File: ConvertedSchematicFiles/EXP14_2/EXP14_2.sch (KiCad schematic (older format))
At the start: 11 parts

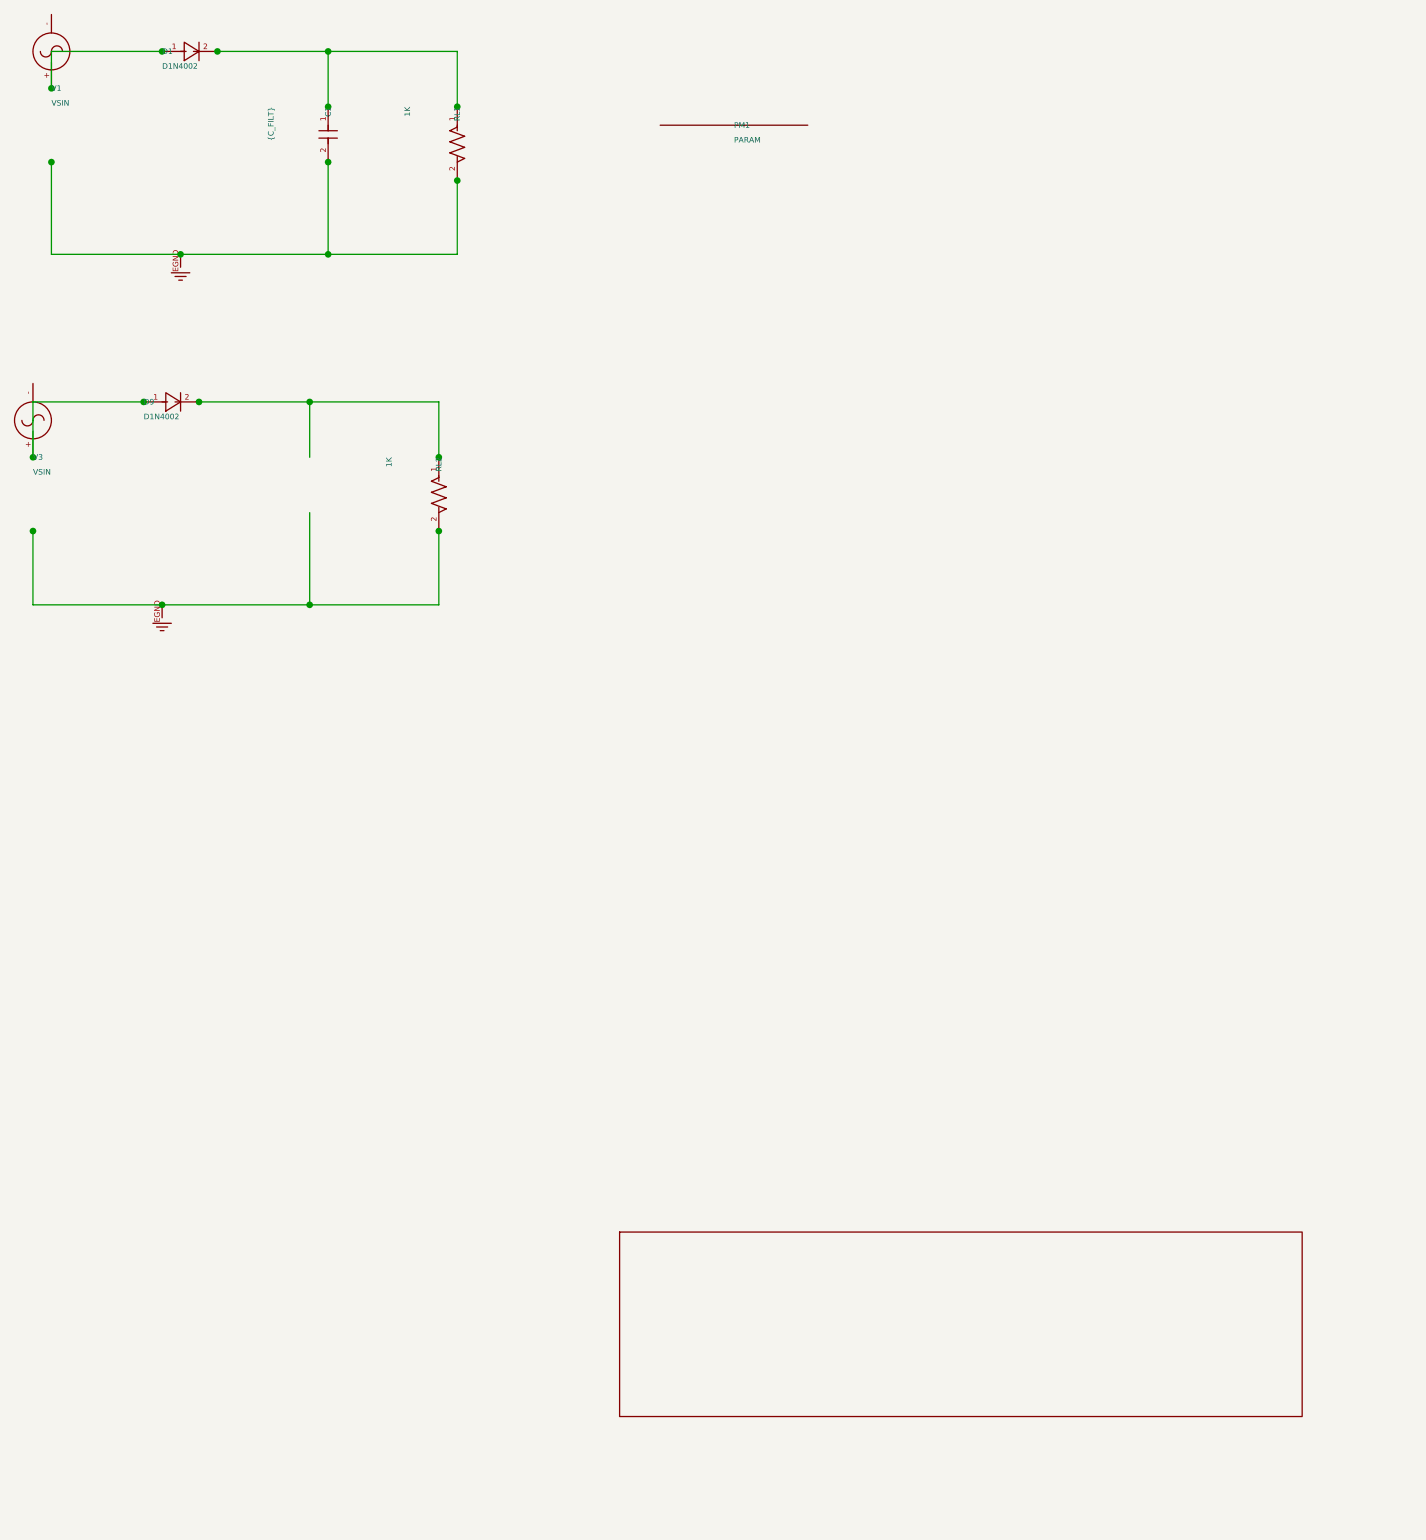
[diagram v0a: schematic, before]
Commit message: Excluded some components. These no longer appear after conversion. When calling shell commands, filenames are in "quotes"
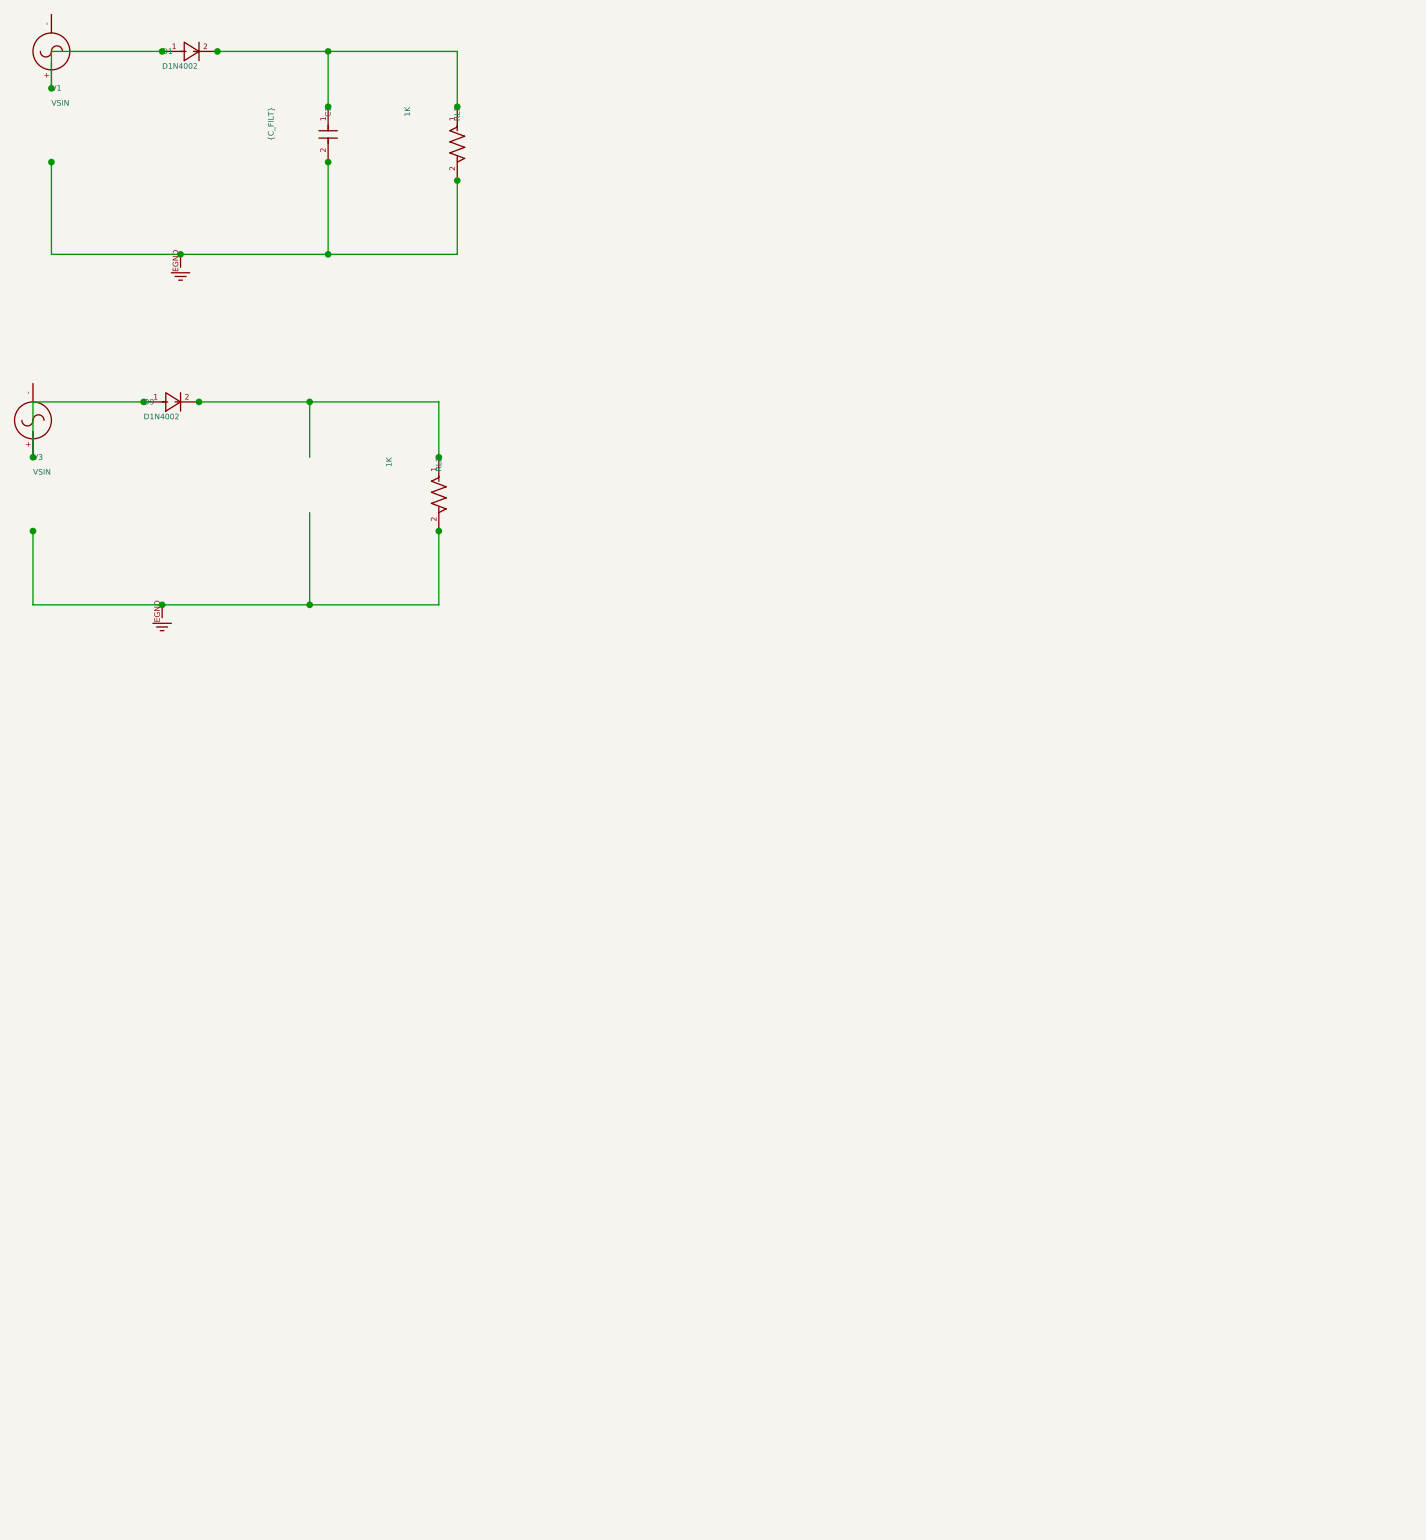
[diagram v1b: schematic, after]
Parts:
- removed PM1: PARAM, symbol PARAM_PSPICE
- removed titleblk: titleblk, symbol TITLEBLK_PSPICE
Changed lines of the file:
@@
-	1    0    0    1
-$EndComp
-$Comp
-L PARAM_PSPICE PM1
-U 1 1 29641421
-P 8800 1400
-F 0 "PM1" H 8800 1400 30  0000 L CNN
-F 1 "PARAM" H 8800 1480 30  0000 L CNN
-	1    8800 1400
-	1    0    0    1
-$EndComp
-$Comp
-L TITLEBLK_PSPICE titleblk
-U 1 1 45202362
-P 11880 8400
-F 0 "titleblk" H 23760 16800 30  0001 L CNN
-F 1 "titleblk" H 23760 16880 30  0001 L CNN
-	1    11880 8400
 	1    0    0    1
 $EndComp

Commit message: Ports issue fixed. Now annotation for ports is #PWR? function added "itos"
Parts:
- removed EGND (x2): EGND, symbol EGND_PSPICE
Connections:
- net labels added: EGND
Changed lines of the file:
@@
 $EndDescr
 $Comp
-L EGND_PSPICE EGND
+L EGND_PSPICE #PWR1
 U 1 1 14289383
 P 5800 2100
-F 0 "EGND" H 11600 4200 30  0001 L CNN
+F 0 "#PWR1" H 11600 4200 30  0001 L CNN
 F 1 "EGND" H 11600 4280 30  0001 L CNN
 	1    5800 2100
@@
 $EndComp
 $Comp
-L EGND_PSPICE EGND
+L EGND_PSPICE #PWR2
 U 1 1 46930886
 P 5700 4000
-F 0 "EGND" H 11400 8000 30  0001 L CNN
+F 0 "#PWR2" H 11400 8000 30  0001 L CNN
 F 1 "EGND" H 11400 8080 30  0001 L CNN
 	1    5700 4000

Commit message: Added LICENSE.txt
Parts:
- V1, V3: value VSIN -> SINE
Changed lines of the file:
@@
 $EndDescr
 $Comp
-L EGND_PSPICE #PWR1
+L GND #PWR1
 U 1 1 14289383
 P 5800 2100
@@
 $EndComp
 $Comp
-L EGND_PSPICE #PWR2
+L GND #PWR2
 U 1 1 46930886
 P 5700 4000
@@
 P 5000 3200
 F 0 "V3" H 5000 3200 30  0000 L CNN
-F 1 "VSIN" H 5000 3280 30  0000 L CNN
+F 1 "SINE" H 5000 3280 30  0000 L CNN
 	1    5000 3200
 	1    0    0    1
@@
 P 5100 1200
 F 0 "V1" H 5100 1200 30  0000 L CNN
-F 1 "VSIN" H 5100 1280 30  0000 L CNN
+F 1 "SINE" H 5100 1280 30  0000 L CNN
 	1    5100 1200
 	1    0    0    1

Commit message: Orientation fix. Library components are now inverted, with +ve y axis going up. In Schematic files, +ve y axis is downwards. This is how the KiCad libraries are. As a result of the above fixed, the converted GND is now oriented correctly.
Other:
- moved on the sheet: V1, V3
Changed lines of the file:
@@
 F 1 "EGND" H 11600 4280 30  0001 L CNN
 	1    5800 2100
-	1    0    0    1
+	1    0    0    -1
 $EndComp
 $Comp
@@
 F 1 "EGND" H 11400 8080 30  0001 L CNN
 	1    5700 4000
-	1    0    0    1
+	1    0    0    -1
 $EndComp
 $Comp
@@
 F 1 "{C_FILT}" H 6600 1610 30  0000 L CNN
 	1    6600 1300
-	0    -1    1    0
+	0    1    1    0
 $EndComp
 $Comp
@@
 F 1 "1K" H 7300 1570 30  0000 L CNN
 	1    7300 1300
-	0    -1    1    0
+	0    1    1    0
 $EndComp
 $Comp
@@
 F 1 "D1N4002" H 5600 2980 30  0000 L CNN
 	1    5600 2900
-	1    0    0    1
+	1    0    0    -1
 $EndComp
 $Comp
@@
 F 1 "SINE" H 5000 3280 30  0000 L CNN
 	1    5000 3200
-	1    0    0    1
+	1    0    0    -1
 $EndComp
 $Comp
@@
 F 1 "1K" H 7200 3470 30  0000 L CNN
 	1    7200 3200
-	0    -1    1    0
+	0    1    1    0
 $EndComp
 $Comp
@@
 F 1 "D1N4002" H 5700 1080 30  0000 L CNN
 	1    5700 1000
-	1    0    0    1
+	1    0    0    -1
 $EndComp
 $Comp
@@
 F 1 "SINE" H 5100 1280 30  0000 L CNN
 	1    5100 1200
-	1    0    0    1
+	1    0    0    -1
 $EndComp
 Wire Wire Line

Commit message: Removed the use of exec, wrote basename function, made integration with eSim easier.
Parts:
- added PM1: PARAM, symbol PARAM_PSPICE
- added titleblk: titleblk, symbol titleblk_PSPICE
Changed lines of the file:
@@
-EESchema Schematic File Version 2  date Saturday 26 June 1999 08:39:42 AM IST
+EESchema Schematic File Version 2  date
 LIBS:power
 LIBS:device
@@
 LIBS:contrib
 LIBS:valves
-LIBS:ConvertedSchematicFiles/EXP14_2-cache
 EELAYER 25  0
 EELAYER END
@@
 Sheet 1 1
 Title ""
-Date "26 Jun 1999"
+Date ""
 Rev ""
 Comp ""
@@
 	1    0    0    -1
 $EndComp
+$Comp
+L PARAM_PSPICE PM1
+U 1 1 29641421
+P 8800 1400
+F 0 "PM1" H 8800 1400 30  0000 L CNN
+F 1 "PARAM" H 8800 1480 30  0000 L CNN
+	1    8800 1400
+	1    0    0    -1
+$EndComp
+$Comp
+L titleblk_PSPICE titleblk
+U 1 1 45202362
+P 11880 8400
+F 0 "titleblk" H 23760 16800 30  0001 L CNN
+F 1 "titleblk" H 23760 16880 30  0001 L CNN
+	1    11880 8400
+	1    0    0    -1
+$EndComp
